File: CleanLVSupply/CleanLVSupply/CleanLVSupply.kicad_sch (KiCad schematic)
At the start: 7 parts, among them J1 12VIN, J2 +-15V, J3 +-15V, J4 5V, J5 5V, J6 5V

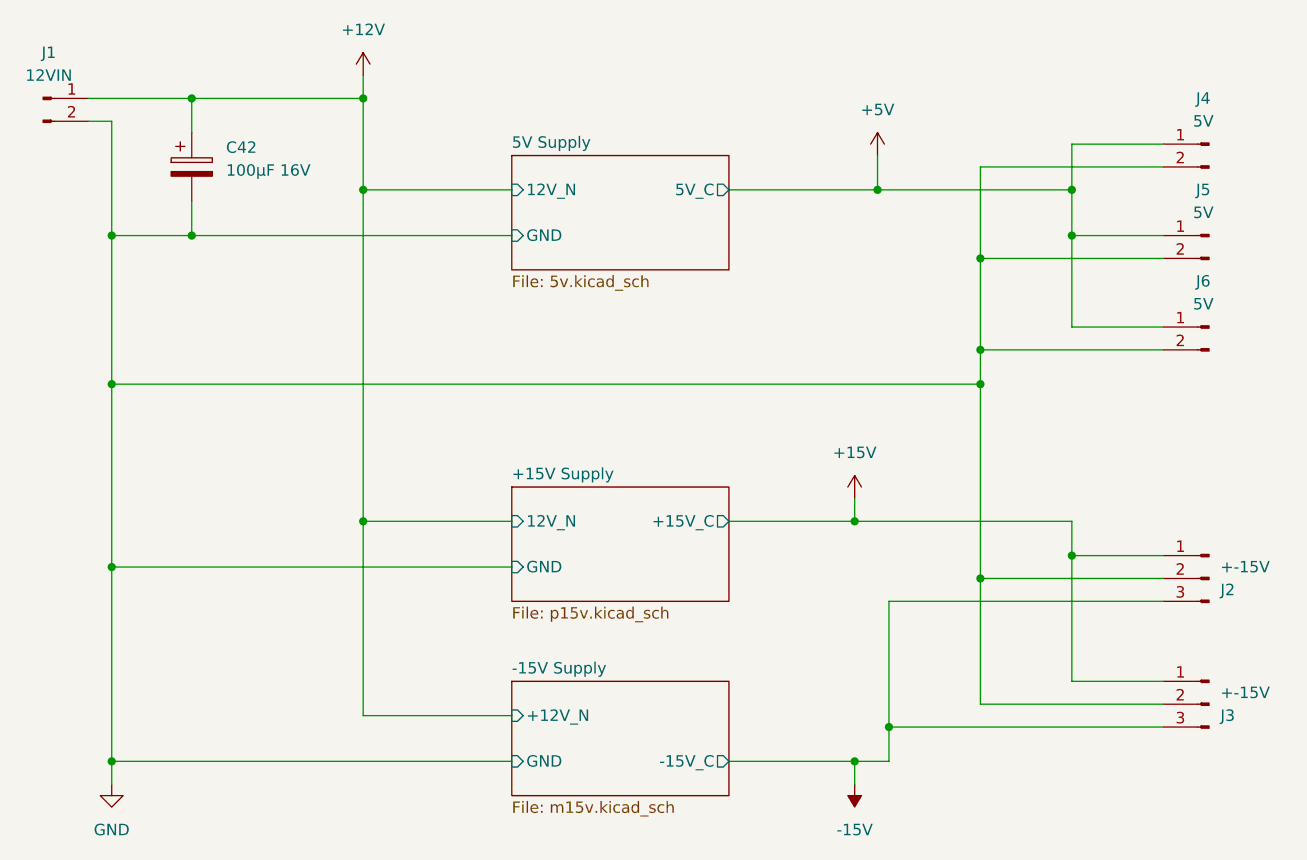
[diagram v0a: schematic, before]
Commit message: CleanLVSupply routing progress
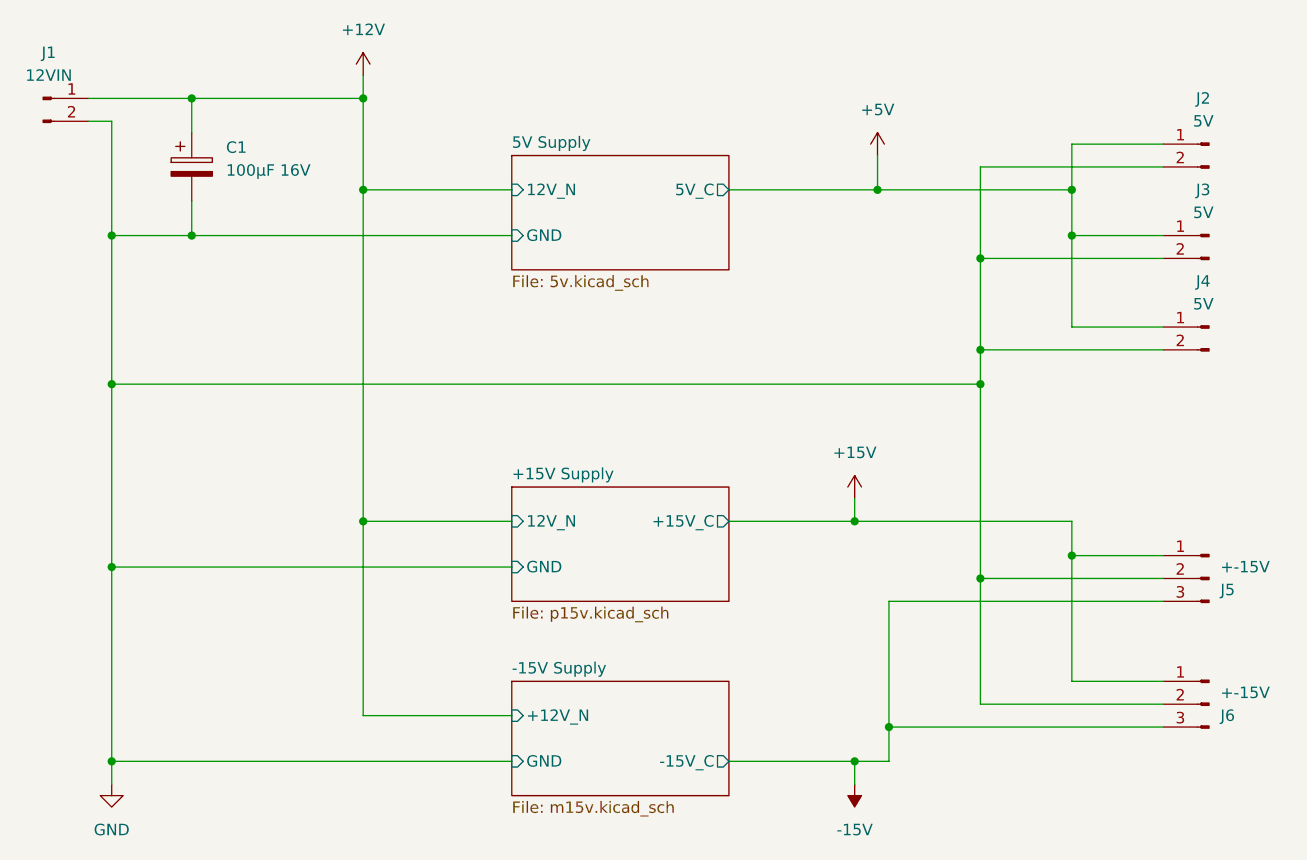
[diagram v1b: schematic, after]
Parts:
- renumbered C42 to C1, J4 to J2, J5 to J3, J6 to J4, J2 to J5, J3 to J6
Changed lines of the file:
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@@
 		(dnp no)
 		(fields_autoplaced yes)
-		(property "Reference" "#PWR04"
+		(property "Reference" "#PWR03"
 			(at 142.24 85.09 0)
 			(effects
@@
 			(project ""
 				(path "/4327ef59-ef76-48f2-90b1-1a9e4399cfc2"
-					(reference "#PWR04")
+					(reference "#PWR03")
 					(unit 1)
 				)
@@
 		(on_board yes)
 		(dnp no)
-		(property "Reference" "J3"
+		(property "Reference" "J6"
 			(at 182.88 105.4101 0)
 			(effects
@@
 			(project "CleanLVSupply"
 				(path "/4327ef59-ef76-48f2-90b1-1a9e4399cfc2"
-					(reference "J3")
+					(reference "J6")
 					(unit 1)
 				)
@@
 		(dnp no)
 		(fields_autoplaced yes)
-		(property "Reference" "#PWR01"
+		(property "Reference" "#PWR04"
 			(at 59.69 119.38 0)
 			(effects
@@
 			(project ""
 				(path "/4327ef59-ef76-48f2-90b1-1a9e4399cfc2"
-					(reference "#PWR01")
+					(reference "#PWR04")
 					(unit 1)
 				)
@@
 		(on_board yes)
 		(dnp no)
-		(property "Reference" "J2"
+		(property "Reference" "J5"
 			(at 182.88 91.4401 0)
 			(effects
@@
 			(project ""
 				(path "/4327ef59-ef76-48f2-90b1-1a9e4399cfc2"
-					(reference "J2")
+					(reference "J5")
 					(unit 1)
 				)
@@
 		(dnp no)
 		(fields_autoplaced yes)
-		(property "Reference" "#PWR02"
+		(property "Reference" "#PWR01"
 			(at 87.63 38.1 0)
 			(effects
@@
 			(project ""
 				(path "/4327ef59-ef76-48f2-90b1-1a9e4399cfc2"
-					(reference "#PWR02")
+					(reference "#PWR01")
 					(unit 1)
 				)
@@
 		(on_board yes)
 		(dnp no)
-		(property "Reference" "J6"
+		(property "Reference" "J4"
 			(at 180.975 57.15 0)
 			(effects
@@
 			(project "CleanLVSupply"
 				(path "/4327ef59-ef76-48f2-90b1-1a9e4399cfc2"
-					(reference "J6")
+					(reference "J4")
 					(unit 1)
 				)
@@
 		(dnp no)
 		(fields_autoplaced yes)
-		(property "Reference" "C42"
+		(property "Reference" "C1"
 			(at 72.39 42.2909 0)
 			(effects
@@
 			(project ""
 				(path "/4327ef59-ef76-48f2-90b1-1a9e4399cfc2"
-					(reference "C42")
+					(reference "C1")
 					(unit 1)
 				)
@@
 		(on_board yes)
 		(dnp no)
-		(property "Reference" "J4"
+		(property "Reference" "J2"
 			(at 180.975 36.83 0)
 			(effects
@@
 			(project "CleanLVSupply"
 				(path "/4327ef59-ef76-48f2-90b1-1a9e4399cfc2"
-					(reference "J4")
+					(reference "J2")
 					(unit 1)
 				)
@@
 		(on_board yes)
 		(dnp no)
-		(property "Reference" "J5"
+		(property "Reference" "J3"
 			(at 180.975 46.99 0)
 			(effects
@@
 			(project "CleanLVSupply"
 				(path "/4327ef59-ef76-48f2-90b1-1a9e4399cfc2"
-					(reference "J5")
+					(reference "J3")
 					(unit 1)
 				)
@@
 		(dnp no)
 		(fields_autoplaced yes)
-		(property "Reference" "#PWR03"
+		(property "Reference" "#PWR02"
 			(at 144.78 46.99 0)
 			(effects
@@
 			(project ""
 				(path "/4327ef59-ef76-48f2-90b1-1a9e4399cfc2"
-					(reference "#PWR03")
-					(unit 1)
-				)
+					(reference "#PWR02")
+					(unit 1)
+				)
